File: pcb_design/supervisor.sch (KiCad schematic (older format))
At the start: 20 parts, among them U5 7400-TSSOP, U6 SN74ALVC08PWR, U7 SN74ALVC08PWR, U8 SN74AUP1G74

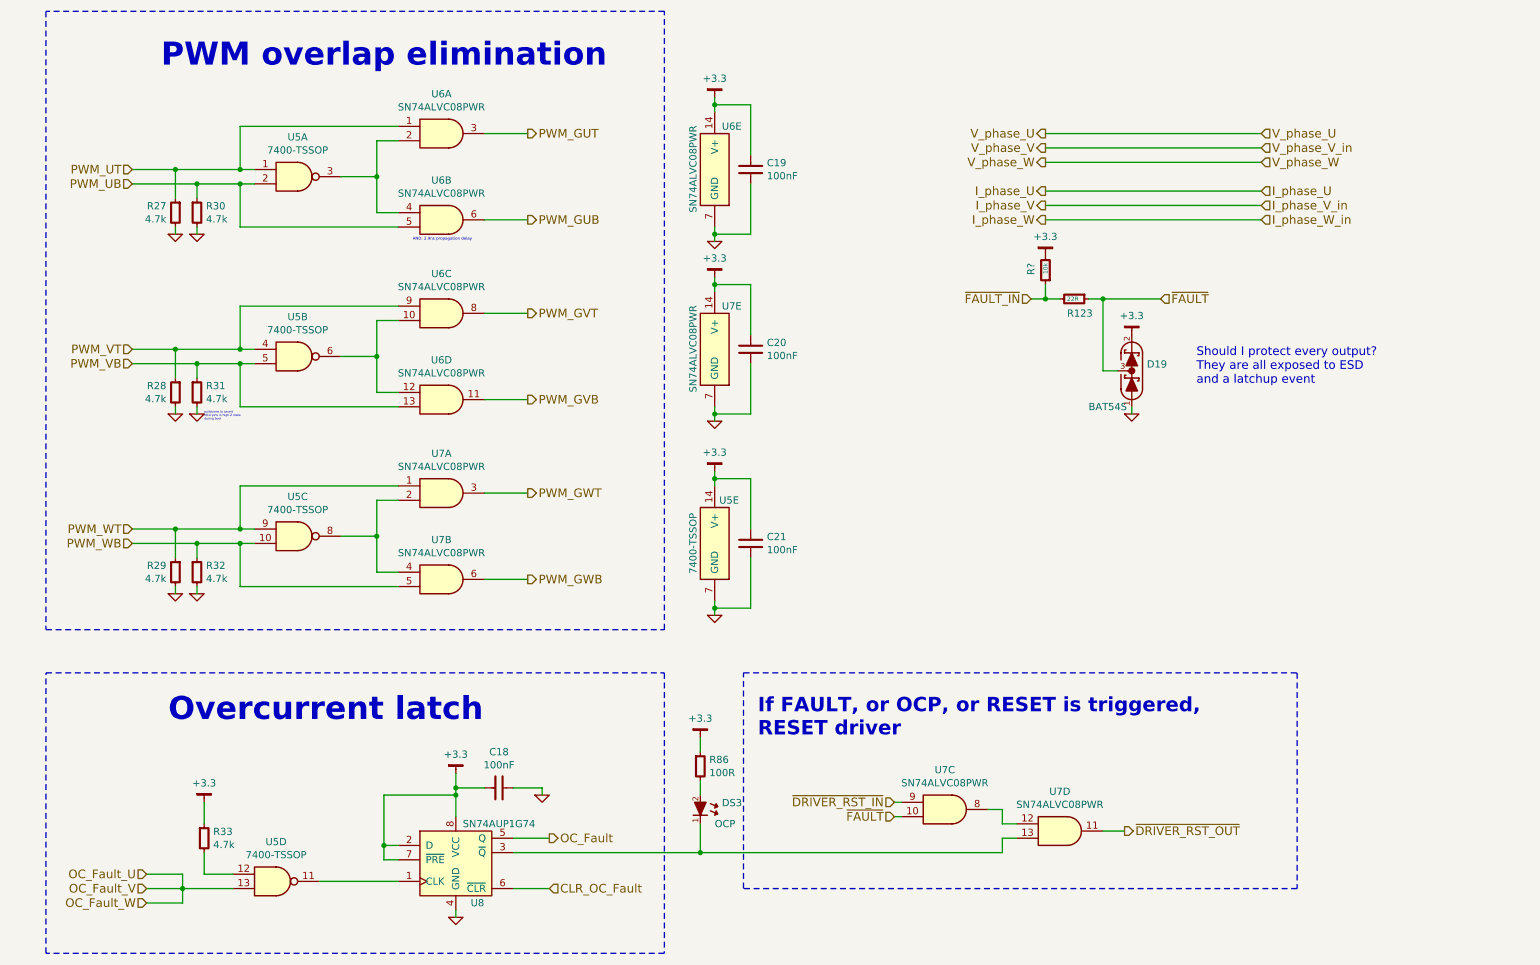
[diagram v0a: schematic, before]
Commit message: Silkscreen logos, fixed swapped OCP inputs, added a button to enter bootloader,missing 3d model.
Signed-off-by: Marcos Chaparro <mchaparro@paltatech.com>
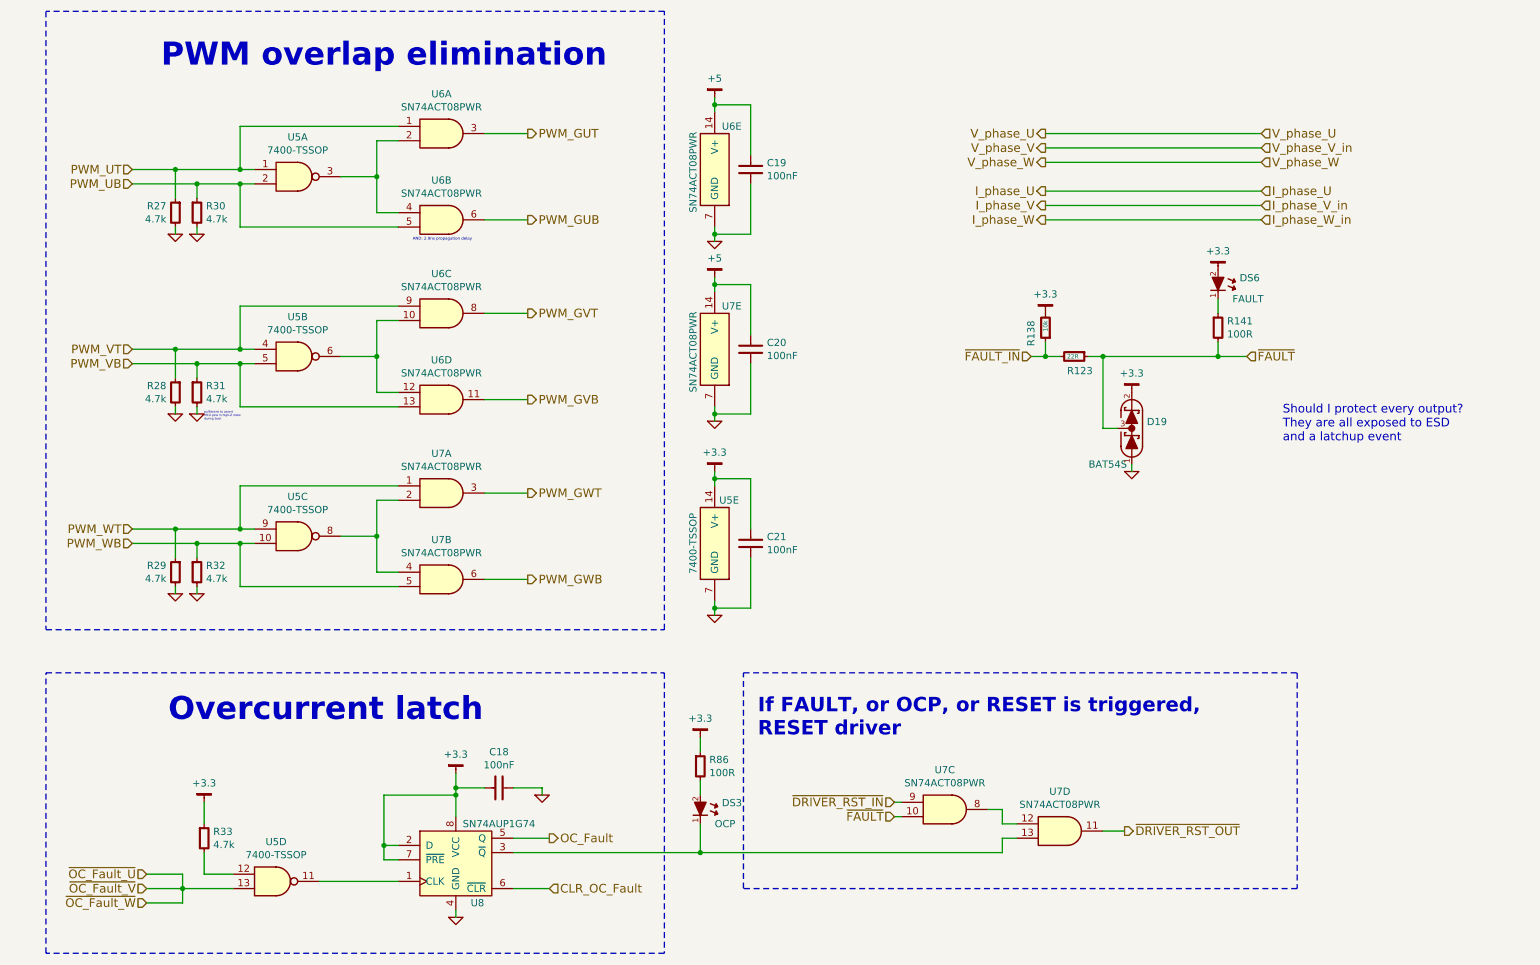
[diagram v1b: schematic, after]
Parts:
- added DS6: FAULT, smd-semi:LED-0603, symbol LED-0603
- added R141: 100R, IPC7351-Nominal:RESC1608X50, symbol R-0603
- U6: value SN74ALVC08PWR -> SN74ACT08PWR; mfg# (none) -> SN74ACT08PWR
- U6, U7: value SN74ALVC08PWR -> SN74ACT08PWR
- gave numbers to parts that had none: 1
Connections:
- net +3.3: now also DS6.2 (A); no longer C19.2, C20.2, U6.14 (V+), U7.14 (V+)
- net ~FAULT: now also R141.2
- net OC_Fault_U renamed ~OC_Fault_U
- new net: DS6.1 (K), R141.1
- new net +5: C19.2, C20.2, U6.14 (V+), U7.14 (V+)
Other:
- moved on the sheet: D19, R123, R138

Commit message: Updated component values according to simulations. 1.5khz for user inputs and  240khz lp pass filters for motor control
Signed-off-by: Marcos Chaparro <mchaparro@paltatech.com>
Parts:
- D19: mfg# (none) -> TBAT54S,LM
- R123: BOM RES SMD 1k 5% [0603] -> RES SMD 22 1% [0603]; mfg# (none) -> RC0603FR-0722RL
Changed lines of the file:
@@
 F 2 "IPC7351-Nominal:RESC1608X50" H 8100 3250 50  0001 C CNN
 F 3 "" H 8100 3300 60  0000 C CNN
-F 4 "RES SMD 1k 5% [0603]" H 8850 3800 60  0001 C CNN "BOM"
+F 4 "RC0603FR-0722RL" H 8100 3250 60  0001 C CNN "mfg#"
+F 5 "RES SMD 22 1% [0603]" H 8850 3800 60  0001 C CNN "BOM"
 	1    8100 3250
 	0    1    1    0
@@
 F 2 "smd-semi:SOT-23" H 8500 3600 60  0001 C CNN
 F 3 "" V 8450 3750 60  0000 C CNN
-F 4 "SCHOTTKY BAT54S" H 8500 3500 60  0001 C CNN "BOM"
+F 4 "TBAT54S,LM" H 8500 3750 60  0001 C CNN "mfg#"
+F 5 "SCHOTTKY BAT54S" H 8500 3500 60  0001 C CNN "BOM"
 	1    8500 3750
 	0    -1   -1   0

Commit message: Completed some part numbers
Signed-off-by: Marcos Chaparro <mchaparro@paltatech.com>
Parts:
- C18, C19, C20, C21: MFR (none) -> Murata Electronics North America; MPN (none) -> GRM188R71E104KA01D; SPN (none) -> 490-1524-1-ND; SPR (none) -> Digikey

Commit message: Completed part number, manufacturer, etc fields. Simulated analog conditioning
Signed-off-by: Marcos Chaparro <mchaparro@paltatech.com>
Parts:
- D19: MFR (none) -> Toshiba Semiconductor and Storage; MPN (none) -> TBAT54S,LM; SPN (none) -> TBAT54SLMCT-ND; SPR (none) -> Digikey
- DS3, DS6: MFR (none) -> Lite-On Inc.; MPN (none) -> LTST-C191KRKT; SPN (none) -> 160-1447-1-ND; SPR (none) -> Digikey
- R123: MFR (none) -> Yageo; MPN (none) -> RC0603FR-0722RL; SPN (none) -> 311-22.0HRCT-ND; SPR (none) -> Digikey
- R138: MFR (none) -> Yageo; MPN (none) -> RC0603FR-0710KL; SPN (none) -> 311-10.0KHRCT-ND; SPR (none) -> Digikey
- R141, R86: MFR (none) -> Yageo; MPN (none) -> RC0603FR-07100RL; SPN (none) -> 311-100HRCT-ND; SPR (none) -> Digikey
- R27, R28, R29, R30, R31, R32, R33: MFR (none) -> Yageo; MPN (none) -> RC0603FR-074K7L; SPN (none) -> 311-4.70KHRCT-ND; SPR (none) -> Digikey
- U5: MFR (none) -> Texas Instruments; MPN (none) -> SN74LVC00APWR; SPN (none) -> 296-1216-1-ND; SPR (none) -> Digikey
- U6, U7: MFR (none) -> Texas Instruments; MPN (none) -> SN74ACT08PWR; SPN (none) -> 296-4355-1-ND; SPR (none) -> Digikey
- U8: MFR (none) -> Texas Instruments; MPN (none) -> SN74AUP1G74DCUR; SPN (none) -> 296-19761-1-ND; SPR (none) -> Digikey

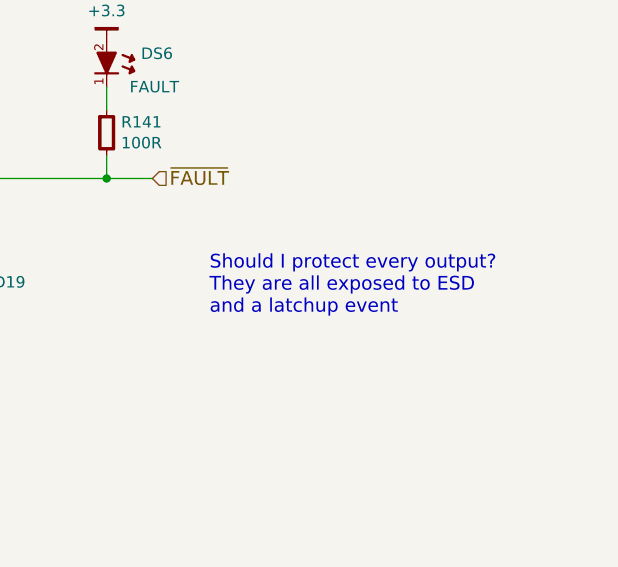
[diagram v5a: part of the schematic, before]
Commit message: Fix inverted diff signals
Signed-off-by: Marcos Chaparro <mchaparro@paltatech.com>
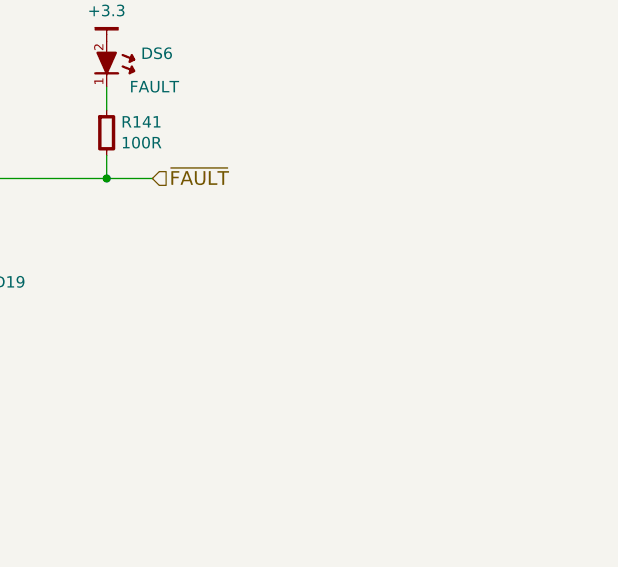
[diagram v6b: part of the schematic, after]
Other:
- note removed: "Should I protect every output?\nThey are all exposed to ESD \nand a latchup event"
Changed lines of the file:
@@
 $Descr A4 11693 8268
 encoding utf-8
-Sheet 7 14
+Sheet 14 14
 Title "Monitor logic"
 Date "2017-02-22"
@@
 Text HLabel 9300 3250 2    60   Input ~ 0
 ~FAULT
-Text Notes 9550 3850 0    60   ~ 0
-Should I protect every output?\nThey are all exposed to ESD \nand a latchup event
 Wire Wire Line
 	9400 1700 7900 1700

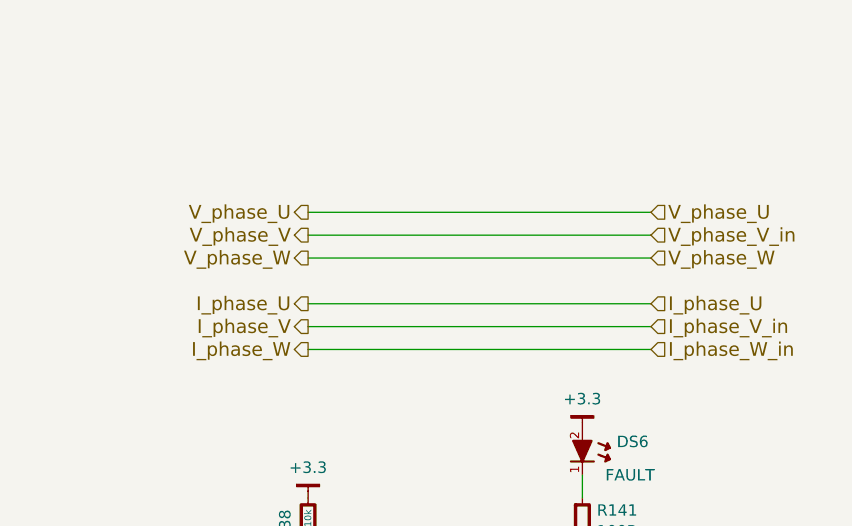
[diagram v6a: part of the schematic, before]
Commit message: Added individual temperature sensing for each half bridge and 2 pwm gpio with low side driver
Signed-off-by: Marcos Chaparro <mchaparro@paltatech.com>
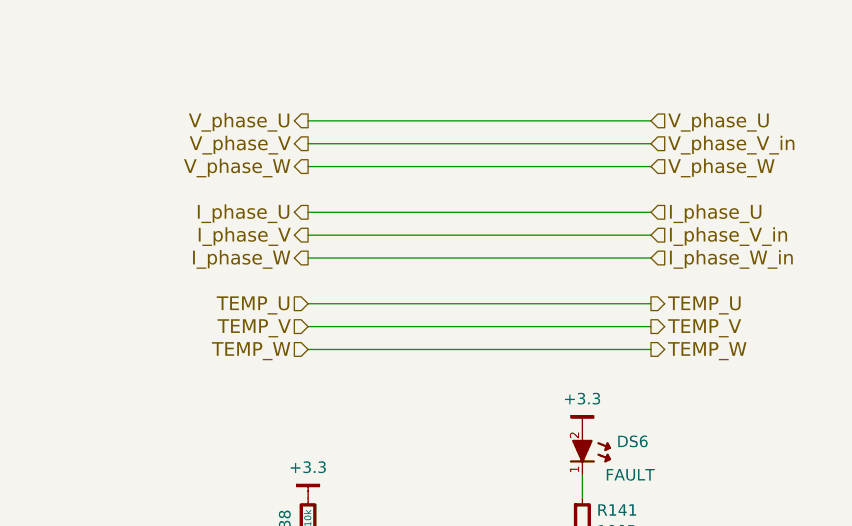
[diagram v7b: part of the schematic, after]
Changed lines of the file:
@@
 $Descr A4 11693 8268
 encoding utf-8
-Sheet 14 14
+Sheet 14 15
 Title "Monitor logic"
 Date "2017-02-22"
@@
 Text HLabel 6850 6450 0    60   Input ~ 0
 ~FAULT
+Text HLabel 9400 1300 2    60   Input ~ 0
+V_phase_U
+Text HLabel 7900 1300 0    60   Output ~ 0
+V_phase_U
+Text HLabel 9400 1400 2    60   Input ~ 0
+V_phase_V_in
+Text HLabel 9400 1500 2    60   Input ~ 0
+V_phase_W
+Text HLabel 7900 1400 0    60   Output ~ 0
+V_phase_V
+Text HLabel 7900 1500 0    60   Output ~ 0
+V_phase_W
 Text HLabel 9400 1700 2    60   Input ~ 0
-V_phase_U
+I_phase_U
 Text HLabel 7900 1700 0    60   Output ~ 0
-V_phase_U
+I_phase_U
 Text HLabel 9400 1800 2    60   Input ~ 0
-V_phase_V_in
+I_phase_V_in
 Text HLabel 9400 1900 2    60   Input ~ 0
-V_phase_W
+I_phase_W_in
 Text HLabel 7900 1800 0    60   Output ~ 0
-V_phase_V
+I_phase_V
 Text HLabel 7900 1900 0    60   Output ~ 0
-V_phase_W
-Text HLabel 9400 2100 2    60   Input ~ 0
-I_phase_U
-Text HLabel 7900 2100 0    60   Output ~ 0
-I_phase_U
-Text HLabel 9400 2200 2    60   Input ~ 0
-I_phase_V_in
-Text HLabel 9400 2300 2    60   Input ~ 0
-I_phase_W_in
-Text HLabel 7900 2200 0    60   Output ~ 0
-I_phase_V
-Text HLabel 7900 2300 0    60   Output ~ 0
 I_phase_W
 Text Notes 1750 1250 0    160  ~ 32
@@
 ~FAULT
 Wire Wire Line
+	9400 1300 7900 1300
+Wire Wire Line
+	9400 1400 7900 1400
+Wire Wire Line
+	7900 1500 9400 1500
+Wire Wire Line
 	9400 1700 7900 1700
 Wire Wire Line
@@
 Wire Wire Line
 	7900 1900 9400 1900
-Wire Wire Line
-	9400 2100 7900 2100
-Wire Wire Line
-	9400 2200 7900 2200
-Wire Wire Line
-	7900 2300 9400 2300
 Wire Wire Line
 	3250 2250 3400 2250
@@
 Connection ~ 7900 3250
 Connection ~ 9100 3250
+Wire Wire Line
+	7900 2100 9400 2100
+Wire Wire Line
+	7900 2200 9400 2200
+Wire Wire Line
+	7900 2300 9400 2300
+Text HLabel 7900 2300 0    60   Input ~ 0
+TEMP_W
+Text HLabel 7900 2200 0    60   Input ~ 0
+TEMP_V
+Text HLabel 7900 2100 0    60   Input ~ 0
+TEMP_U
+Text HLabel 9400 2100 2    60   Output ~ 0
+TEMP_U
+Text HLabel 9400 2200 2    60   Output ~ 0
+TEMP_V
+Text HLabel 9400 2300 2    60   Output ~ 0
+TEMP_W
 $EndSCHEMATC

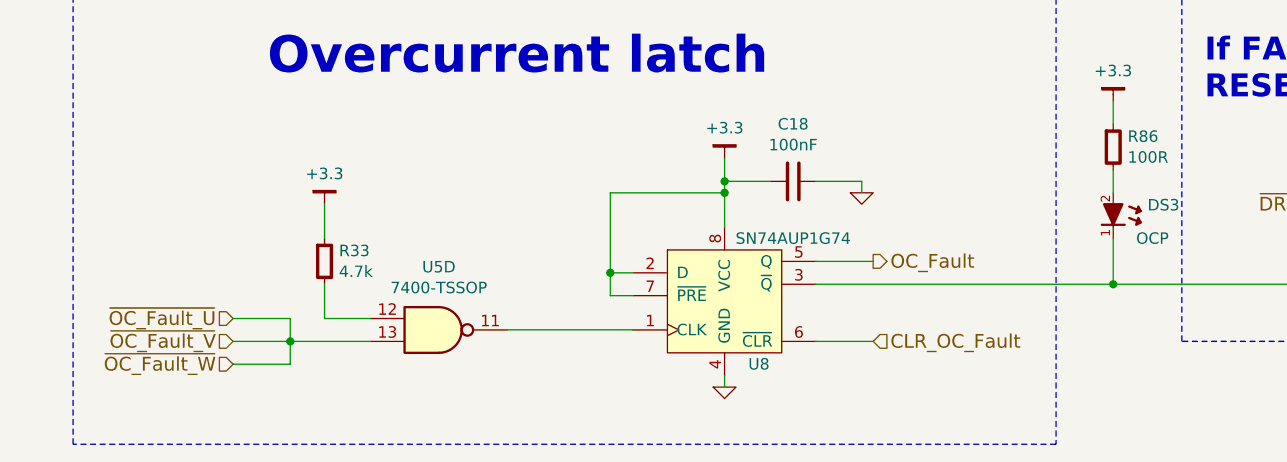
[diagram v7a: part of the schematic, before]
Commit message: Fixed power supply inductor footprints in the layout
Signed-off-by: Marcos Chaparro <mchaparro@paltatech.com>
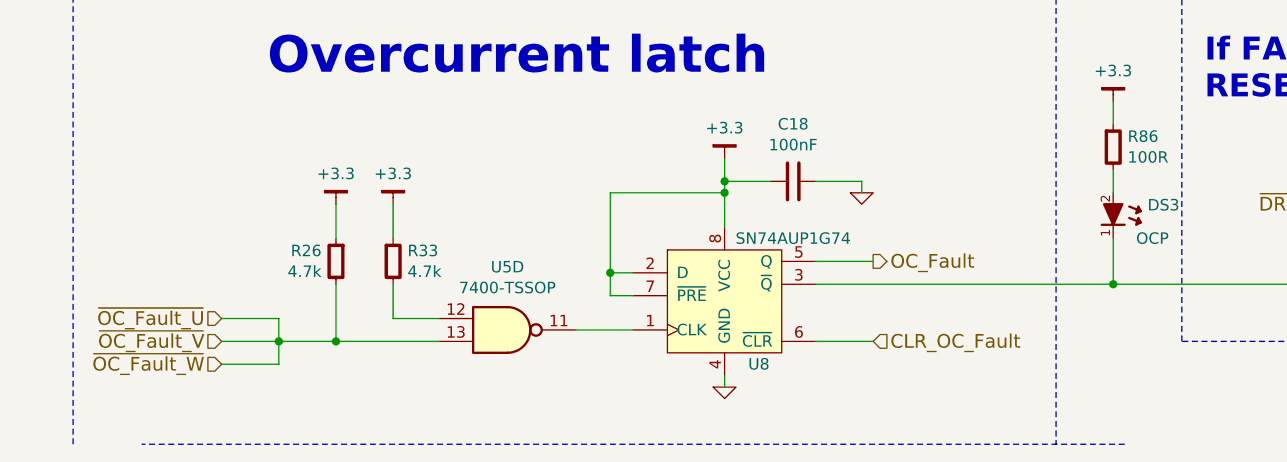
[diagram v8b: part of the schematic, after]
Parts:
- added R26: 4.7k, IPC7351-Nominal:RESC1608X50, symbol R-0603
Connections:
- net +3.3: now also R26.1
- net ~OC_Fault_U: now also R26.2
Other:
- moved on the sheet: R33, U5D
